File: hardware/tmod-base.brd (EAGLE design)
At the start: 65 x 56 mm, 96 parts, among them IC1 TPS70933, IC10 TPS70933, IC2 INA219SOT, IC3 STM32L052C8T6, IC4 HX1, IC5 LMP7702, IC6 TPS62143, IC8 TPS22918, IC9 BME280, J1 DNP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

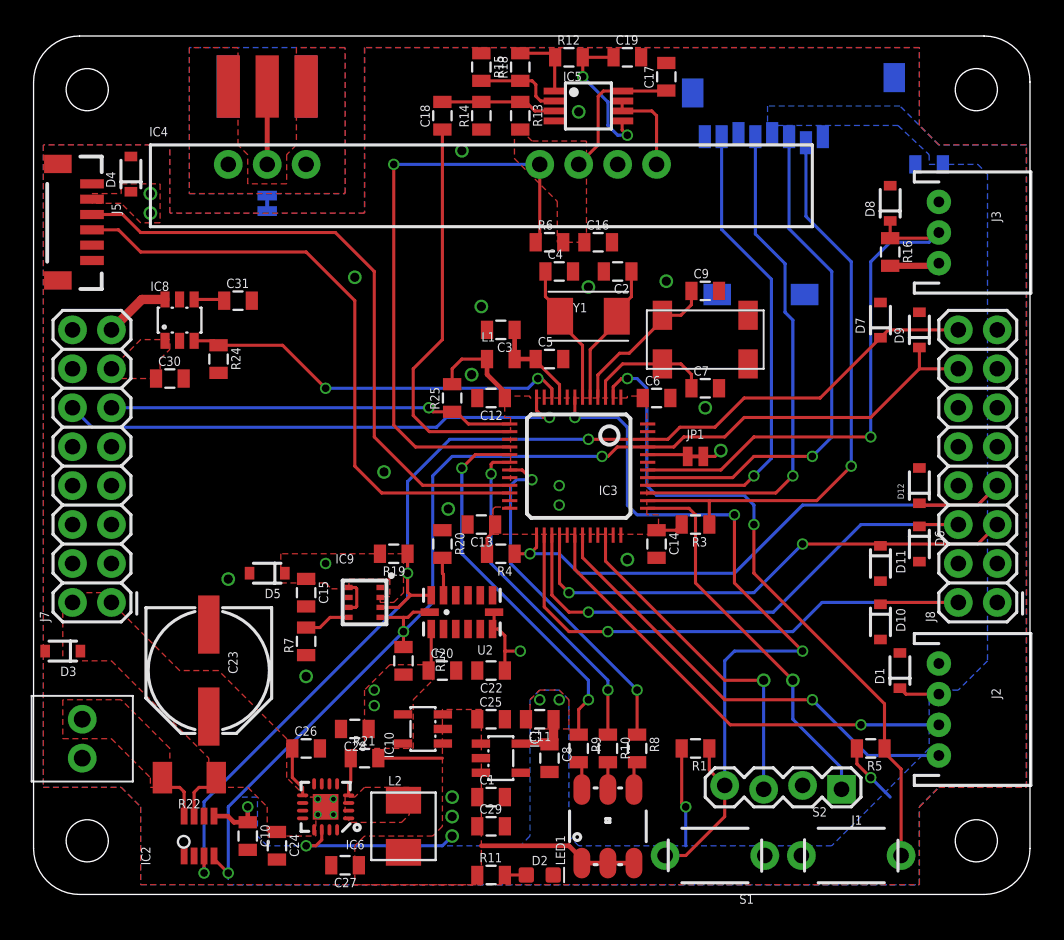
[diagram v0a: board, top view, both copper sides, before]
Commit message: Add silkscreen to HAB base board
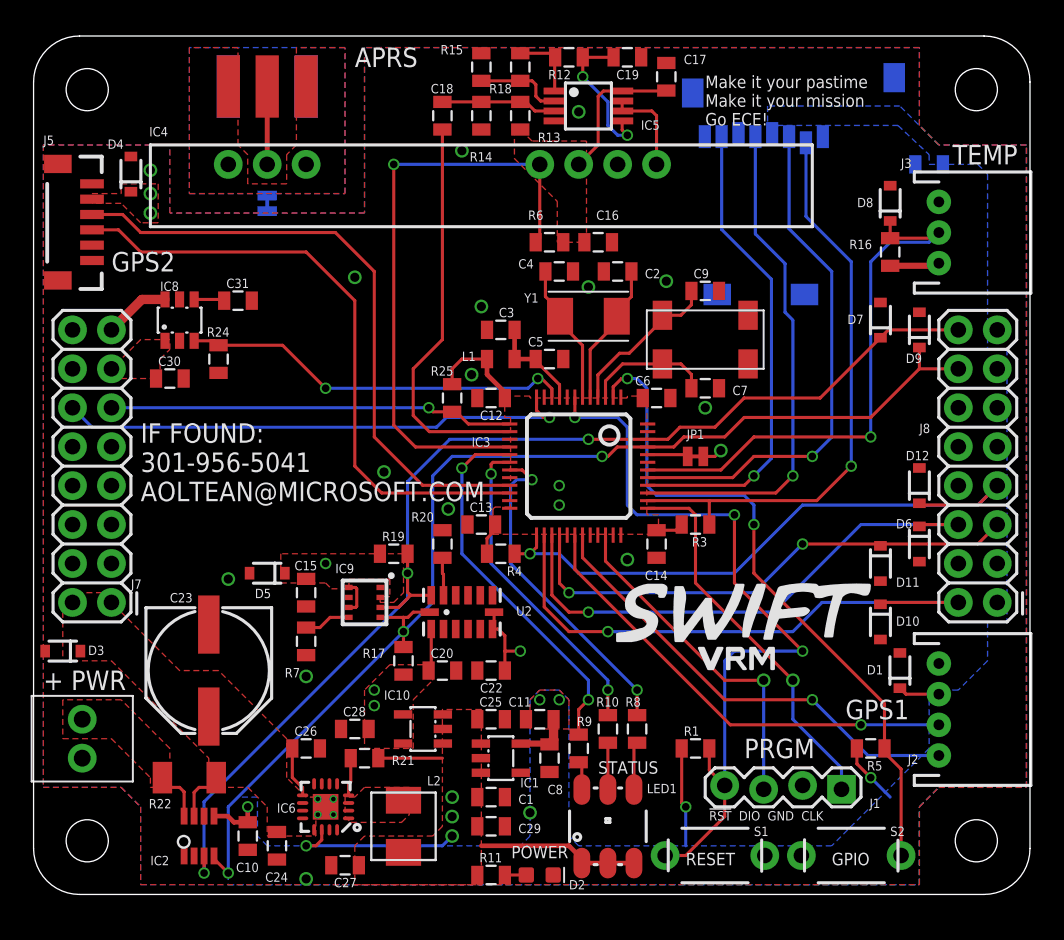
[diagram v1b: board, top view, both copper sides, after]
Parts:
- added U$1: (no value), HAB:MSFT_LOGO
- added U$2: (no value), HAB:GARAGE
- added U$3: (no value), HAB:SWIFT
- D2: value GREEN -> POWER
- LED1: value COM-10866 -> STATUS
- moved R10 1.27 mm to (37.5, 10.8)
- moved R8 1.27 mm to (39.4, 10.8)
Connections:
- net 3.3V: no longer J8.3
- net 5V: now also J8.3
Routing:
- net LEDR: track 22.1 -> 20.8 mm
- net LEDB: track 22.9 -> 21.7 mm
- net RC: track 1.78 -> 3.05 mm
- net BC: track 1.86 -> 3.13 mm
- net GND: vias 18 -> 21
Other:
- board text added: "!RST! DIO GND CLK"
- board text added: "+ PWR"
- board text added: "- +"
- board text added: "APRS"
- board text added: "BAT GND RXI 5V 5SW"
- board text added: "BAT GND TXO GND GND"
- board text added: "GND GND MOSI CS VS GND 3.3"
- board text added: "GPIO"
- board text added: "IF FOUND: 301-956-5041 AOLTEAN@MICROSOFT.COM"
- board text added: "Make it your pastime Make it your mission Go ECE!"
- board text added: "Maker Garage Project Phoenix REV B"
- board text added: "PRGM"
- board text added: "RESET"
- board text added: "SCK GND MISO GND GND SCL SDA"

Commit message: Started work on Pi and Edison example application cards, neither is complete
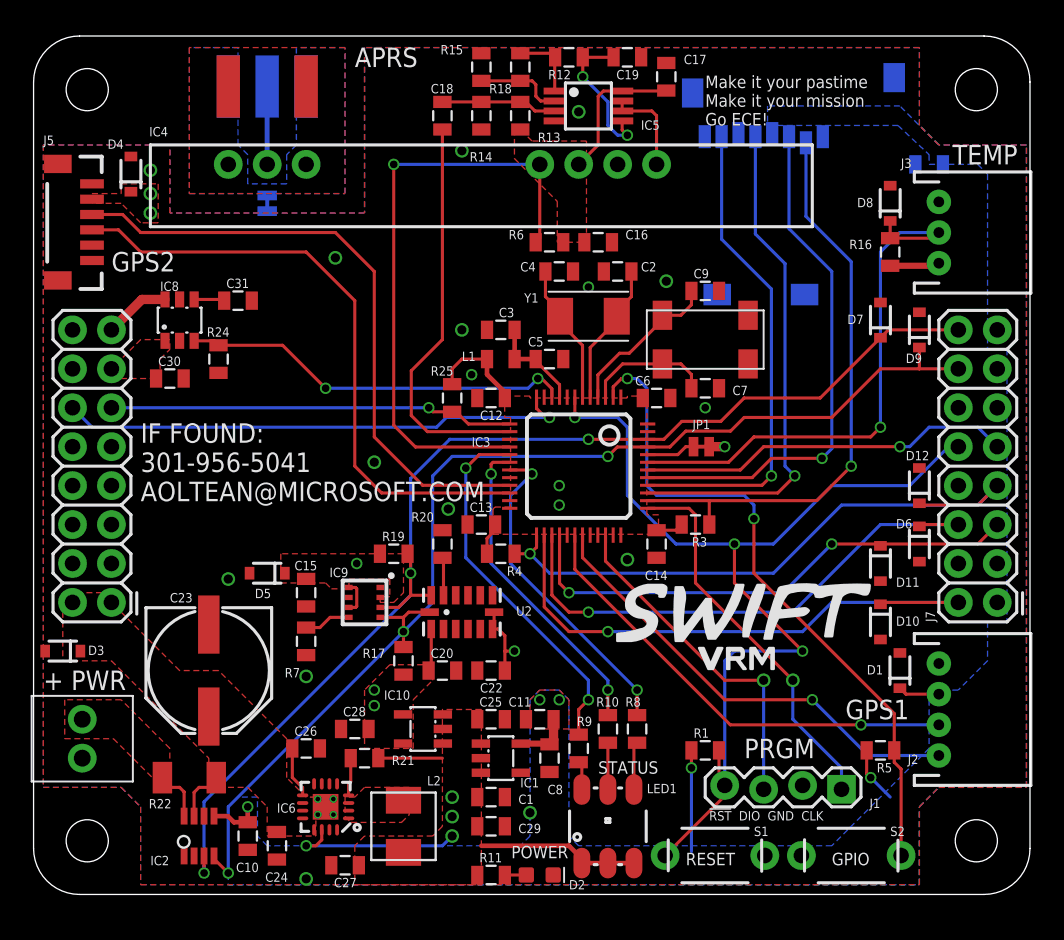
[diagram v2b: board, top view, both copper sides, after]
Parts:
- removed J8: STACK2, SparkFun-Connectors:2X8
- J7: value STACK1 -> HAB-EXP; device SparkFun-Connectors:2X8 -> HAB:HAB-EXP
- moved J7 18.0 mm to (2.54, 36.8), turned to 270 degrees
- moved J$1 5.08 mm to (17.8, 52.7), flipped to the bottom
- moved U$1 2.62 mm to (37.5, 34.3)
- moved JP1 0.74 mm to (43.6, 29.2)
- moved R1 0.65 mm to (43.8, 9.40)
- moved R5 0.65 mm to (55.2, 9.40)
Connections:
- new net RSV7: IC3.42, J7.B9
- net !RST!: now also J7.B10
- net 3.3V: now also J7.B15; no longer J8.15
- net 5V: now also J7.A13, J7.B3; no longer J7.13, J8.3
- net 5V_PI: now also J7.A15; no longer J7.15
- net GND: now also J7.A14, J7.A16, J7.A4, J7.A9, J7.B1, J7.B12, J7.B13, J7.B4, J7.B8; no longer J7.14, J7.16, J7.4, J7.9, J8.1, J8.12, J8.13, J8.4, J8.8
- net LCS: now also J7.B7; no longer J8.7
- net MISO2: now also J7.B6; no longer J8.6
- net MOSI2: now also J7.B5; no longer J8.5
- net R_RX: now also J7.A11; no longer J7.11
- net R_TX: now also J7.A12; no longer J7.12
- net SCK2: now also J7.B2; no longer J8.2
- net SCL: now also J7.B14; no longer J8.14
- net SDA: now also J7.B16; no longer J8.16
- net TEMP: now also IC3.43; no longer IC3.42
- net VBAT: now also J7.A1, J7.A2; no longer J7.1, J7.2
- net VS: now also J7.B11; no longer J8.11
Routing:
- net RSV7: track 0.00 -> 24.5 mm, vias 0 -> 1
- net !RST!: track 51.3 -> 65.9 mm
- net MISO1: track 31.1 -> 31.8 mm
- net BOOT0: track 2.66 -> 3.21 mm
- added copper zone on layer 15, net RGND
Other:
- board text added: "GND 5V MOSI CS IRQ VS GND 3.3"
- board text added: "SCK GND MISO GND !RST! GND SCL SDA"
- board text removed: "GND GND MOSI CS VS GND 3.3"
- board text removed: "SCK GND MISO GND GND SCL SDA"

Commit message: Continued work on the Pi-style application board
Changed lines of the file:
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@@
 <contactref element="S2" pad="2"/>
 <contactref element="R5" pad="1"/>
-<wire x1="56.5912" y1="2.54" x2="56.5912" y2="8.1788" width="0.2032" layer="1"/>
-<wire x1="56.5912" y1="8.1788" x2="56.145" y2="8.625" width="0.2032" layer="1"/>
-<wire x1="56.145" y1="9.398" x2="56.145" y2="8.625" width="0.2032" layer="1"/>
+<wire x1="56.5912" y1="2.54" x2="56.5912" y2="7.5438" width="0.2032" layer="1"/>
+<wire x1="56.5912" y1="7.5438" x2="56.145" y2="7.99" width="0.2032" layer="1"/>
+<wire x1="56.145" y1="9.398" x2="56.145" y2="7.99" width="0.2032" layer="1"/>
 <wire x1="37.81" y1="32.44" x2="37.81" y2="33.111" width="0.2032" layer="1"/>
 <wire x1="37.81" y1="33.111" x2="38.354" y2="33.655" width="0.2032" layer="1"/>
@@
 <wire x1="37.465" y1="13.97" x2="29.845" y2="21.59" width="0.2032" layer="16"/>
 <wire x1="29.845" y1="21.59" x2="29.845" y2="27.432" width="0.2032" layer="16"/>
-<wire x1="31.06" y1="28.19" x2="29.968" y2="28.19" width="0.2032" layer="1"/>
+<wire x1="31.06" y1="28.19" x2="30.095" y2="28.19" width="0.2032" layer="1"/>
 <via x="29.845" y="27.432" extent="1-16" drill="0.5"/>
-<wire x1="29.845" y1="27.432" x2="29.845" y2="28.067" width="0.2032" layer="1"/>
-<wire x1="29.845" y1="28.067" x2="29.968" y2="28.19" width="0.2032" layer="1"/>
+<wire x1="29.845" y1="27.432" x2="29.845" y2="27.94" width="0.2032" layer="1"/>
+<wire x1="29.845" y1="27.94" x2="30.095" y2="28.19" width="0.2032" layer="1"/>
 </signal>
 <signal name="TXD">
@@
 <wire x1="47.625" y1="29.21" x2="56.515" y2="29.21" width="0.2032" layer="1"/>
 <wire x1="62.865" y1="29.21" x2="61.595" y2="30.48" width="0.2032" layer="16"/>
-<wire x1="61.595" y1="30.48" x2="58.42" y2="30.48" width="0.2032" layer="16"/>
-<wire x1="58.42" y1="30.48" x2="57.15" y2="29.21" width="0.2032" layer="16"/>
-<wire x1="57.15" y1="29.21" x2="56.515" y2="29.21" width="0.2032" layer="16"/>
+<wire x1="61.595" y1="30.48" x2="57.785" y2="30.48" width="0.2032" layer="16"/>
 <via x="56.515" y="29.21" extent="1-16" drill="0.5"/>
+<wire x1="57.785" y1="30.48" x2="56.515" y2="29.21" width="0.2032" layer="16"/>
 </signal>
 </signals>

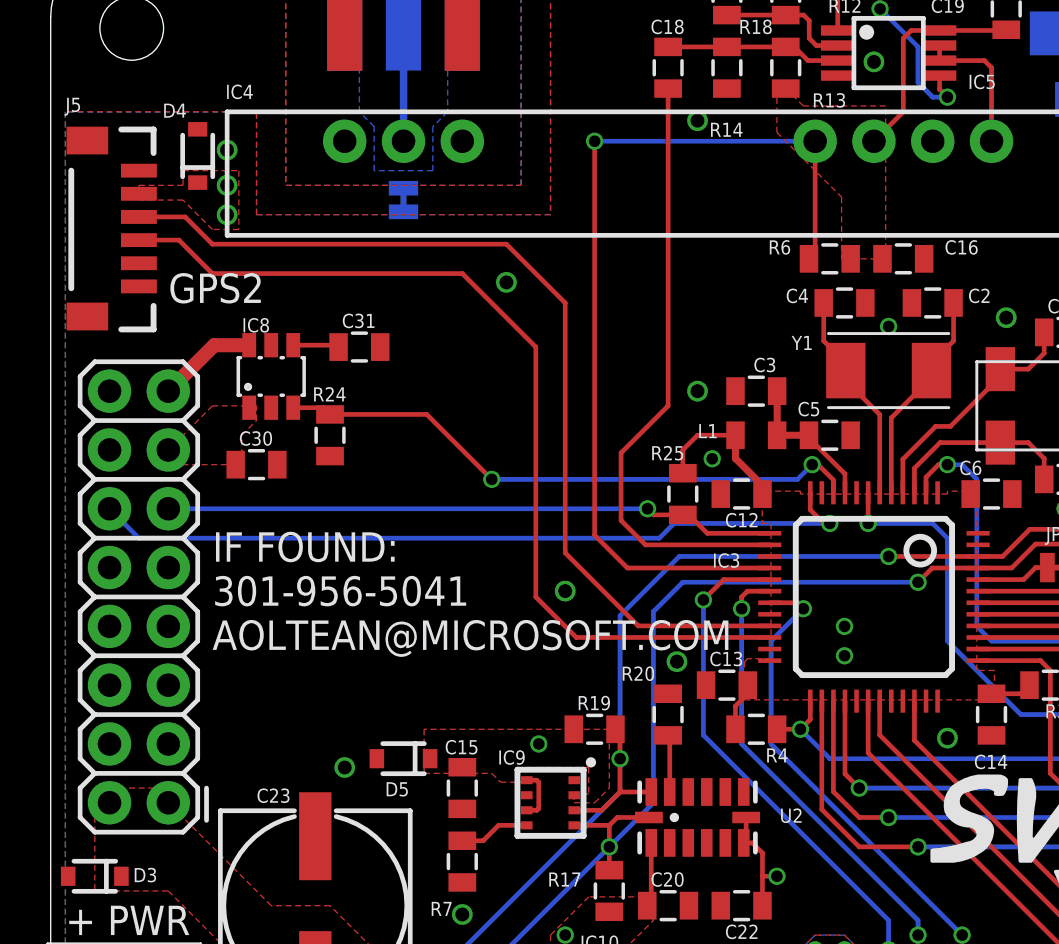
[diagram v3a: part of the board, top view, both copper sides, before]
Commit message: Route out RSV5 and RSV6 to microcontroller pins
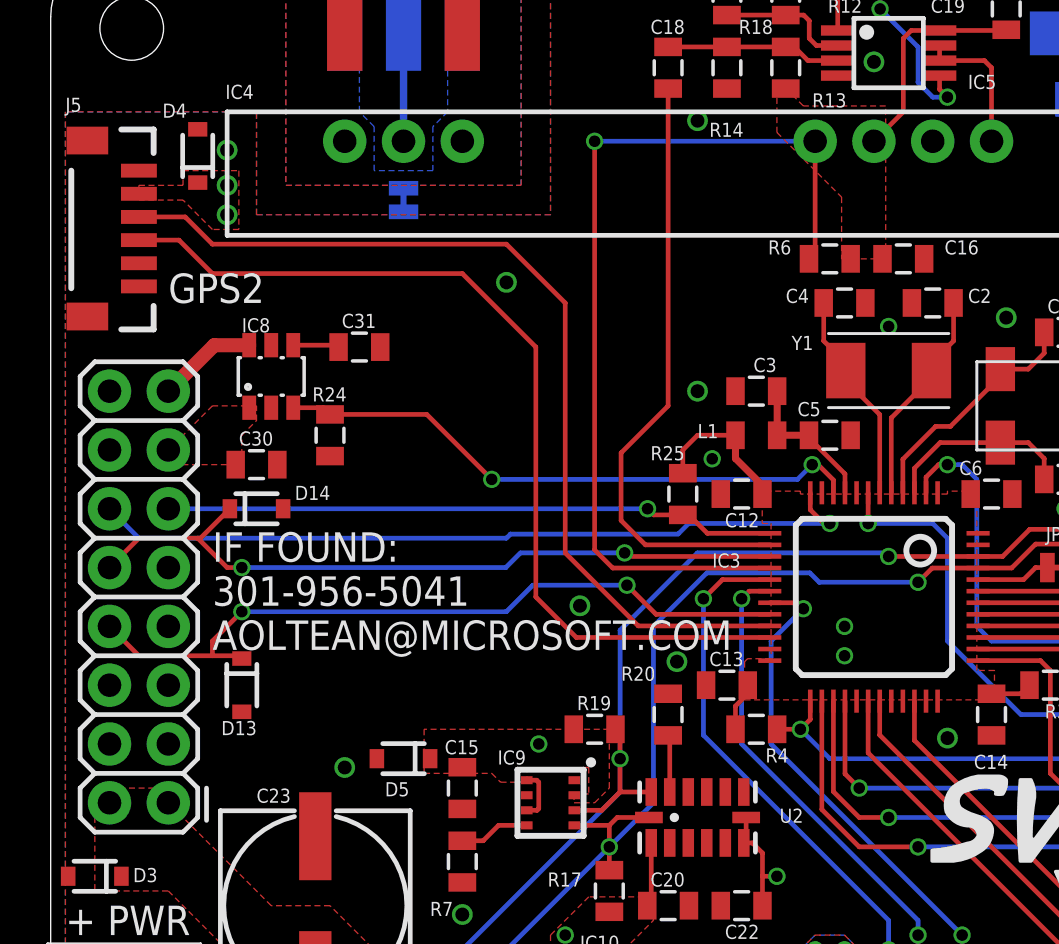
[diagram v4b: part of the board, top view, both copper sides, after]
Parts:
- added D13, D14: 5.6V, SparkFun-DiscreteSemi:SOD-323
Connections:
- removed net RFU1: IC3.15
- removed net RFU2: IC3.20
- new net RSV5: D13.C, IC3.20, J7.A8
- new net RSV6: D14.C, IC3.15, J7.A10
- net GND: now also D13.A, D14.A
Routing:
- net RSV5: track 0.00 -> 32.5 mm, vias 0 -> 2
- net RSV6: track 0.00 -> 31.8 mm, vias 0 -> 2
